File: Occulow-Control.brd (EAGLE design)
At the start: 38.1 x 101.6 mm, 40 parts, among them J1 CORTEX_DEBUG_PTH, T1 DMP3010LK3, T2 DMP3010LK3, T3 DMP3010LK3

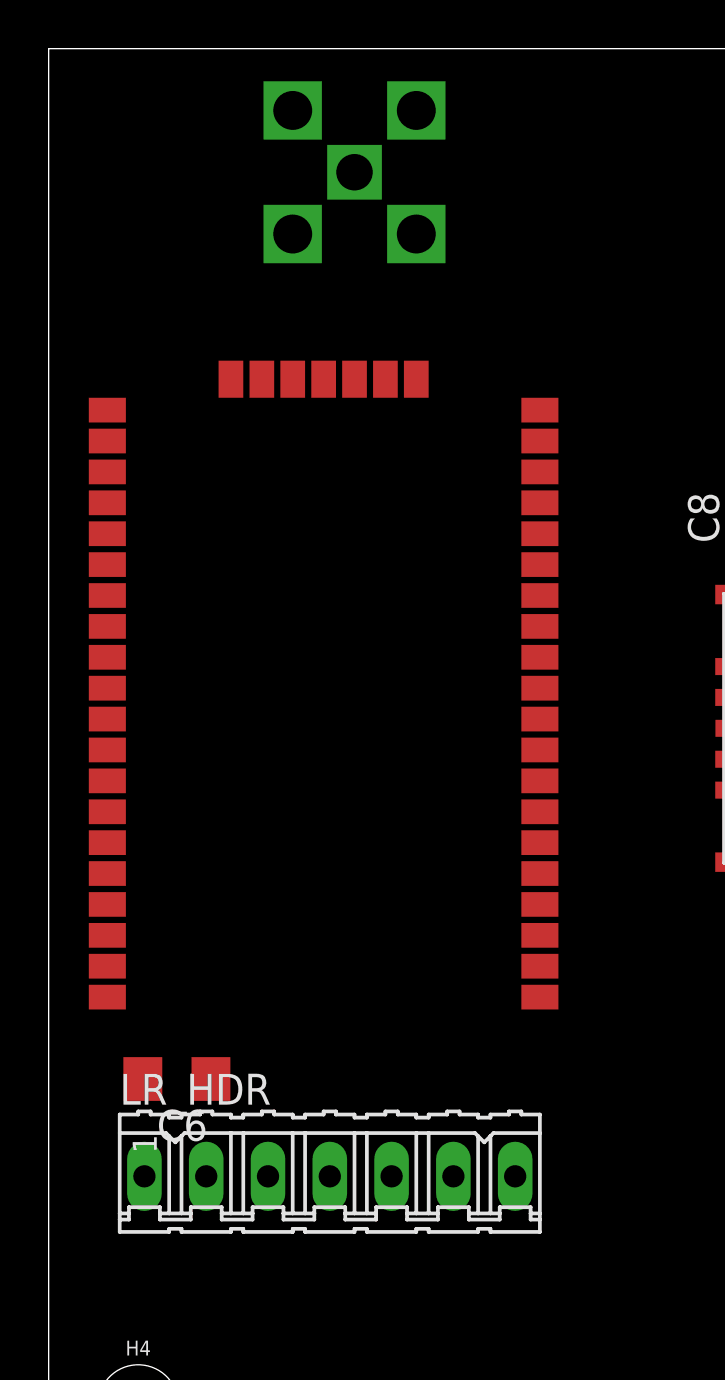
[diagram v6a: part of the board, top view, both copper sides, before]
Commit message: Lora routed
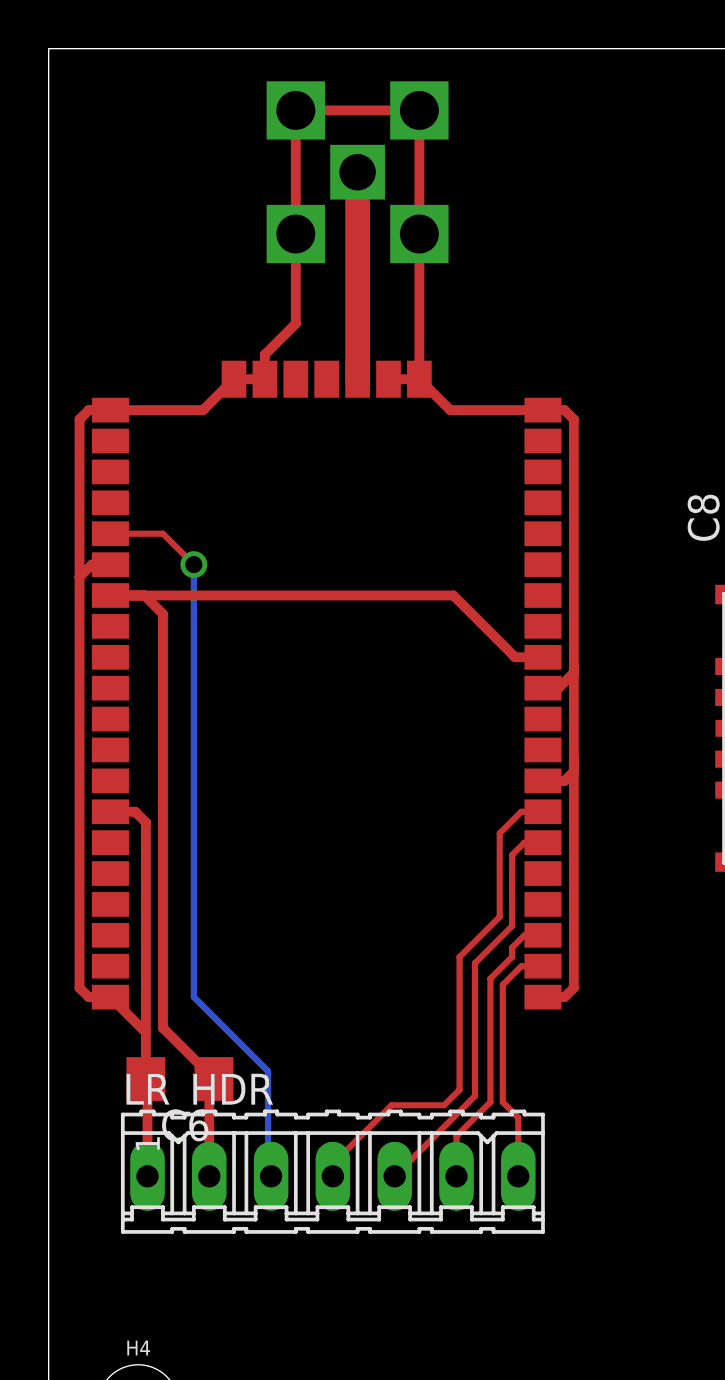
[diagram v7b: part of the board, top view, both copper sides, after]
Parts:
- moved C6 0.13 mm to (5.40, 59.2)
- moved LR_HDR 0.13 mm to (11.7, 55.2)
- moved U$2 0.13 mm to (11.4, 74.0)
- moved U$3 0.13 mm to (12.7, 96.5)
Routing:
- net LR_GND: track 0.00 -> 117.4 mm
- net LR_VCC: track 0.00 -> 45.4 mm
- net LR_RST_N: track 0.00 -> 30.4 mm, vias 0 -> 1
- net LR_RX: track 0.00 -> 20.3 mm
- net LR_TX: track 0.00 -> 16.7 mm
- net LR_CTS: track 0.00 -> 11.8 mm
- net LR_RTS: track 0.00 -> 10.1 mm
- net RF: track 0.00 -> 8.51 mm

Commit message: All routed
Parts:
- moved R5 1.89 mm to (28.6, 57.5)
- moved C9 1.70 mm to (33.9, 57.5)
- moved R2 0.72 mm to (29.2, 64.0)
- moved R3 0.52 mm to (34.2, 64.0)
- moved R4 0.52 mm to (31.6, 64.0)
- moved C8 0.25 mm to (28.6, 82.5)
- moved U$4 0.25 mm to (31.5, 73.7)
- moved C10 0.25 mm to (33.4, 81.2)
- moved SL1 0.25 mm to (33.4, 89.5)
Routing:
- net GR_VCC: track 0.00 -> 67.5 mm, vias 0 -> 1
- net GR_SCL: track 0.00 -> 52.7 mm
- net GR_GND: track 0.00 -> 40.1 mm, vias 0 -> 1
- net GR_INT: track 0.00 -> 33.9 mm, vias 0 -> 1
- net GR_SDA: track 0.00 -> 31.8 mm
- net N$2: track 0.00 -> 16.7 mm
- net N$4: track 0.00 -> 8.27 mm
- net N$3: track 0.00 -> 5.41 mm
- net LR_GND: track 117.4 -> 119.3 mm
